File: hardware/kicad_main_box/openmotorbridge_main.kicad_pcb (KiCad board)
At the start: 4 copper layers, 85 x 55 mm, 40 parts, among them J1 DEUTSCH_DTM12_HEADER_SMD, J2 MicroSD_Card, J3 USB2_IDC_HEADER_9PIN, J4 RGB_LED_3PIN, J5 PWR_BAT_NTC_4PIN, SW1 SW_PAIR_RESET, U1 LM5164-Q1, U2 ESP32-S3-WROOM-1U-N16R8, U3 ES8388_Codec, U5 BMI270_IMU, U6 TCAN334G, U7 SX1262IMLTRT, U8 DW3110, U9 TPS7A0533_LDO, Y1_UWB 38.4MHz

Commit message: hardware(main-box): replace J1 open pinheader with official shrouded IDC box header (Wannenstecker)
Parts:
- J1: value DEUTSCH_DTM12_HEADER_SMD -> DEUTSCH_DTM12_IDC_HEADER; footprint Connector_PinHeader_2.54mm:PinHeader_2x06_P2.54mm_Vertical_SMD -> Connector_IDC:IDC-Header_2x06_P2.54mm_Vertical

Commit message: feat(audio): genuinely integrate Qualcomm QCC3084 BT 5.4 Audio SoC for dual-helmet aptX HD link
- Hardware (PCBA 01): Placed U9 (Qualcomm QCC3084 module with onboard ceramic antenna) at (175, 106) on F.Cu; wired I2S bus, UART, and reset/enable controls in mcu_codec_can.kicad_sch.
- Firmware: Upgraded bluetooth_audio_manager to full QCC3084 driver supporting Dual-A2DP aptX HD/Adaptive, LE Audio Auracast, independent AVRCP volume, and modal HFP 1.8 telephony interceptor.
- Docs: Updated 02_intercom_matrix_profiles, 07_pcba_hardware_pinouts, and 09_firmware_architecture with technical specs and pinout tables for the dedicated Qualcomm audio link.
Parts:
- added U9: QCC3084_BT54_AUDIO, RF_Module:Qualcomm_QCC3084_Module, F.Cu at (175.0, 106.0)
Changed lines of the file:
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@@
+		)
+	)
+	(footprint "RF_Module:Qualcomm_QCC3084_Module"
+		(layer "F.Cu")
+		(at 175 106)
+		(descr "Qualcomm QCC3084 Bluetooth 5.4 Audio SoC Module (Dual-A2DP aptX-HD, LE Audio Auracast, HFP 1.8), 13x18mm with integrated ceramic antenna")
+		(tags "Qualcomm QCC3084 Bluetooth 5.4 aptX HD Audio Module")
+		(property "Reference" "U9"
+			(at 0 -10.2 0)
+			(layer "F.SilkS")
+			(effects
+				(font
+					(size 0.8 0.8)
+					(thickness 0.12)
+				)
+			)
+		)
+		(property "Value" "QCC3084_BT54_AUDIO"
+			(at 0 10.2 0)
+			(layer "F.Fab")
+			(effects
+				(font
+					(size 0.8 0.8)
+					(thickness 0.12)
+				)
+			)
+		)
+		(property "Datasheet" "https://www.qualcomm.com/products/application/audio/qcc3084"
+			(at 0 0 0)
+			(layer "F.Fab")
+			(hide yes)
+			(effects
+				(font
+					(size 1.27 1.27)
+				)
+			)
+		)
+		(property "Description" "Qualcomm QCC3084 Dual-A2DP aptX HD / LE Audio Auracast BT 5.4 Module"
+			(at 0 0 0)
+			(layer "F.Fab")
+			(hide yes)
+			(effects
+				(font
+					(size 1.27 1.27)
+				)
+			)
+		)
+		(property "LCSC" "C983084"
+			(at 0 0 0)
+			(layer "F.SilkS")
+			(effects
+				(font
+					(size 1.27 1.27)
+					(thickness 0.15)
+				)
+			)
+		)
+		(attr smd)
+		(duplicate_pad_numbers_are_jumpers no)
+		(fp_rect
+			(start -6.5 -9)
+			(end 6.5 9)
+			(stroke
+				(width 0.15)
+				(type solid)
+			)
+			(fill no)
+			(layer "F.SilkS")
+		)
+		(fp_rect
+			(start 3.5 -8)
+			(end 6 -4.5)
+			(stroke
+				(width 0.12)
+				(type solid)
+			)
+			(fill yes)
+			(layer "F.SilkS")
+		)
+		(fp_rect
+			(start -6.8 -9.3)
+			(end 6.8 9.3)
+			(stroke
+				(width 0.05)
+				(type solid)
+			)
+			(fill no)
+			(layer "F.CrtYd")
+		)
+		(fp_text user "CERAMIC_ANT"
+			(at 4.75 -2.5 90)
+			(layer "F.SilkS")
+			(effects
+				(font
+					(size 0.6 0.6)
+					(thickness 0.1)
+				)
+			)
+		)
+		(fp_text user "${REFERENCE}"
+			(at 0 0 0)
+			(layer "F.Fab")
+			(effects
+				(font
+					(size 0.8 0.8)
+					(thickness 0.12)
+				)
+			)
+		)
+		(pad "1" smd rect
+			(at -6.2 -6)
+			(size 1.4 0.8)
+			(layers "F.Cu" "F.Mask" "F.Paste")
+			(net "VCC_3V3")
+		)
+		(pad "2" smd rect
+			(at -6.2 -4)
+			(size 1.4 0.8)
+			(layers "F.Cu" "F.Mask" "F.Paste")
+			(net "GND_PWR")
+		)
+		(pad "3" smd rect
+			(at -6.2 -2)
+			(size 1.4 0.8)
+			(layers "F.Cu" "F.Mask" "F.Paste")
+			(net "I2S_MCLK")
+		)
+		(pad "4" smd rect
+			(at -6.2 0)
+			(size 1.4 0.8)
+			(layers "F.Cu" "F.Mask" "F.Paste")
+			(net "I2S_BCLK")
+		)
+		(pad "5" smd rect
+			(at -6.2 2)
+			(size 1.4 0.8)
+			(layers "F.Cu" "F.Mask" "F.Paste")
+			(net "I2S_WS")
+		)
+		(pad "6" smd rect
+			(at -6.2 4)
+			(size 1.4 0.8)
+			(layers "F.Cu" "F.Mask" "F.Paste")
+			(net "I2S_DOUT")
+		)
+		(pad "7" smd rect
+			(at -6.2 6)
+			(size 1.4 0.8)
+			(layers "F.Cu" "F.Mask" "F.Paste")
+			(net "I2S_DIN")
+		)
+		(pad "8" smd rect
+			(at 6.2 6)
+			(size 1.4 0.8)
+			(layers "F.Cu" "F.Mask" "F.Paste")
+			(net "GND_PWR")
+		)
+		(pad "9" smd rect
+			(at 6.2 4)
+			(size 1.4 0.8)
+			(layers "F.Cu" "F.Mask" "F.Paste")
+			(net "BT_UART_TX")
+		)
+		(pad "10" smd rect
+			(at 6.2 2)
+			(size 1.4 0.8)
+			(layers "F.Cu" "F.Mask" "F.Paste")
+			(net "BT_UART_RX")
+		)
+		(pad "11" smd rect
+			(at 6.2 0)
+			(size 1.4 0.8)
+			(layers "F.Cu" "F.Mask" "F.Paste")
+			(net "BT_EN")
+		)
+		(pad "12" smd rect
+			(at 6.2 -2)
+			(size 1.4 0.8)
+			(layers "F.Cu" "F.Mask" "F.Paste")
+			(net "GND_PWR")
+		)
+		(embedded_fonts no)
+		(model "${KICAD10_3DMODEL_DIR}/RF_Module.3dshapes/Raytac_MDBT50Q.step"
+			(offset
+				(xyz 0 0 0)
+			)
+			(scale
+				(xyz 1.25 1 1.2)
+			)
+			(rotate
+				(xyz 0 0 0)
+			)
 		)
 	)

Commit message: hardware(cartridge): move ES8388 audio codec to B.Cu bottom layer to eliminate overlaps and isolate from actuator MOSFETs
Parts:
- moved ANT2 17.6 mm to (169.2, 99.7)
- moved U9 6.75 mm to (181.4, 104.0)
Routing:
- net GND_SHIELD: track 0.00 -> 171.1 mm, vias 0 -> 4
- net I2S_WS: track 0.00 -> 7.18 mm
- net USB_D_N: track 0.00 -> 3.96 mm
- net I2S_BCLK: track 0.00 -> 3.11 mm
- net POD2_VCC: track 0.00 -> 2.60 mm
- net VCC_5V: track 0.00 -> 2.04 mm
- net I2S_DOUT: track 0.00 -> 0.71 mm
- net I2S_DIN: track 0.00 -> 0.71 mm

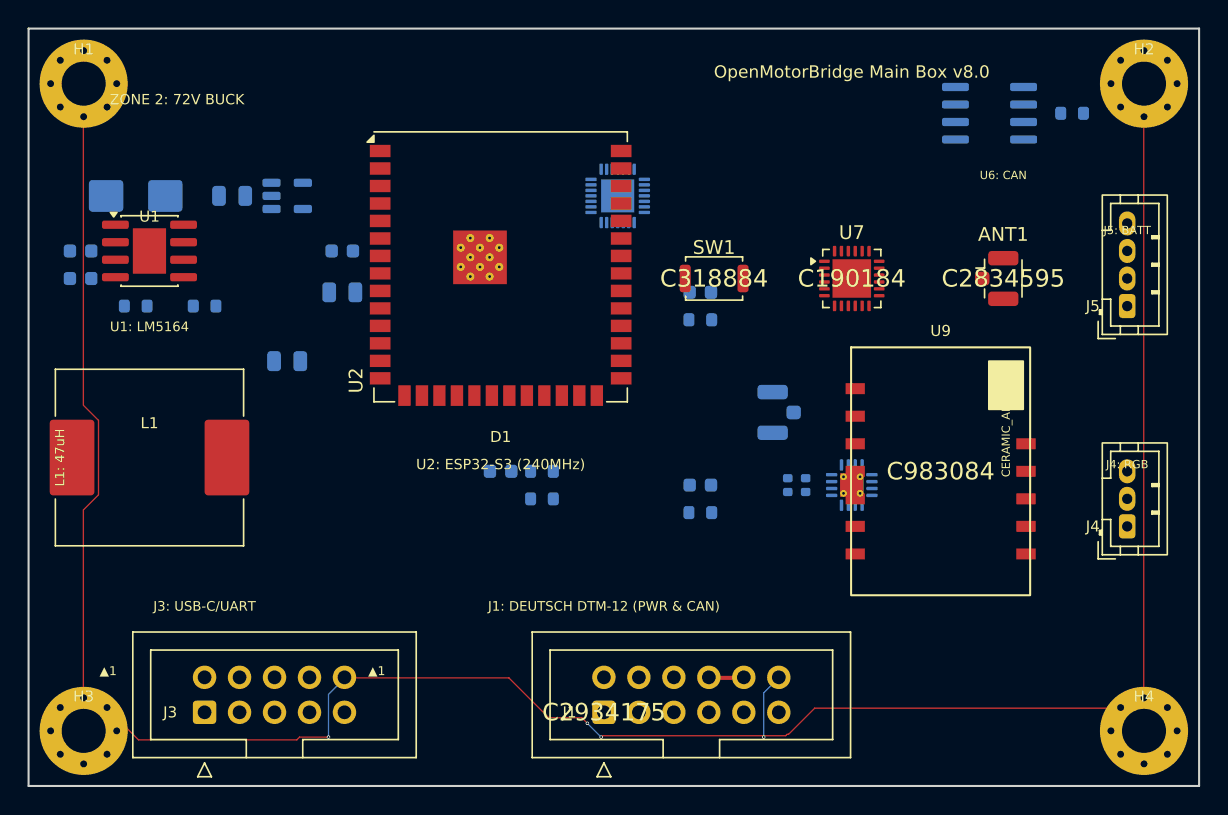
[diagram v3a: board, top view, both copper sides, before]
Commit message: fix(main_box): clean up schematics, connect LoRa/UWB/IMU/SD/LED nets, verify J2 MicroSD placement
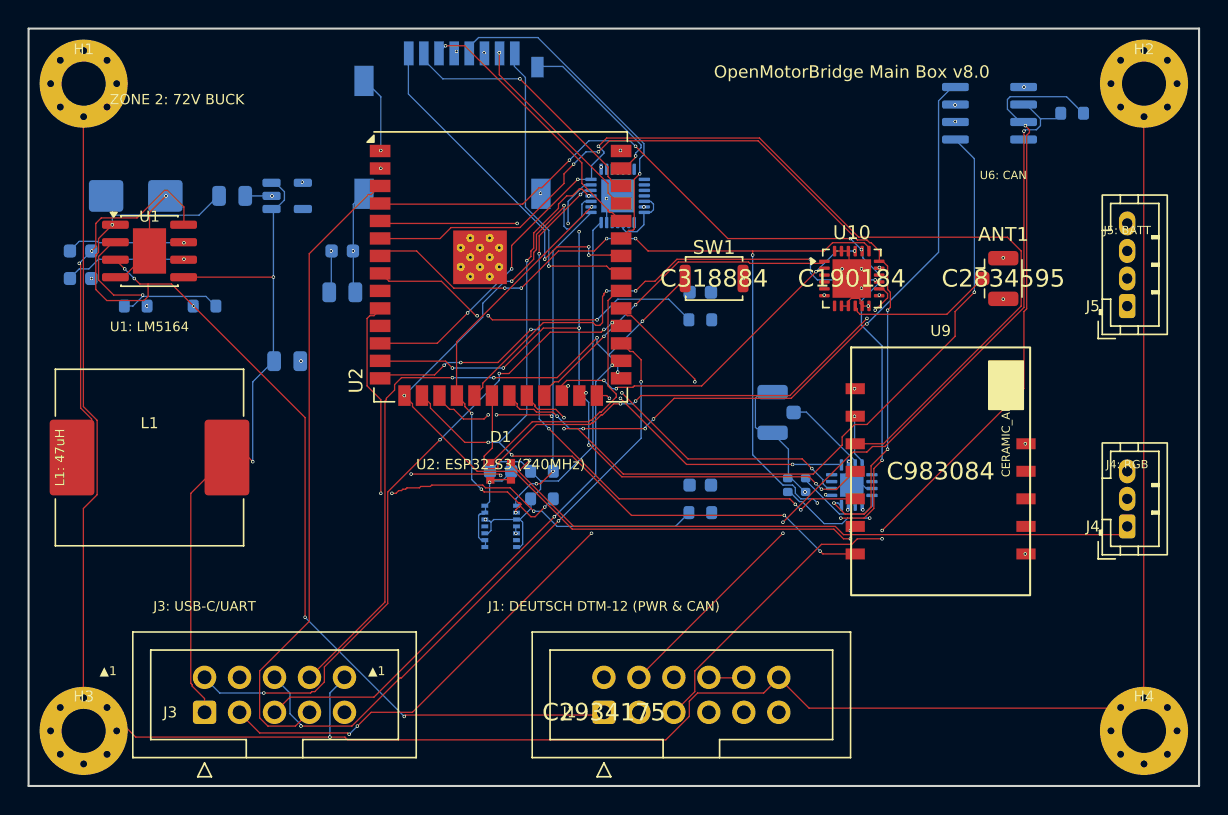
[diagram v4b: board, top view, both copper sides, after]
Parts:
- J2: footprint Connector_Card:microSD_HC_Molex_47571-0001 -> Connector_Card:microSD_HC_Hirose_DM3D-SF
- moved J2 22.5 mm to (146.0, 79.0), turned to 180 degrees
- renumbered U7 to U10, U9 to U11
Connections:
- ANT1 pad 1: (no net) -> LORA_RF_868
- ANT1 pad 2: (no net) -> GND_PWR
- ANT2 pad 1: (no net) -> UWB_RF_CH5
- ANT2 pad 2: (no net) -> GND_PWR
- SW1 pad 1: (no net) -> ESP_BOOT
- SW1 pad 2: (no net) -> GND_PWR
- U10 pad : (no net) -> GND_PWR
- U10 pad 1: (no net) -> LORA_RST
- U10 pad 10: (no net) -> LORA_RF_868
- U10 pad 11: (no net) -> GND_PWR
- U10 pad 12: (no net) -> GND_PWR
- U10 pad 13: (no net) -> VCC_3V3
- U10 pad 14: (no net) -> LORA_BUSY
- U10 pad 15: (no net) -> LORA_DIO1
- U10 pad 16: (no net) -> LORA_DIO2
- U10 pad 17: (no net) -> VCC_3V3
- U10 pad 18: (no net) -> SPI_MISO
- U10 pad 19: (no net) -> SPI_MOSI
- U10 pad 2: (no net) -> LORA_XTA
- U10 pad 20: (no net) -> SPI_SCK
- U10 pad 21: (no net) -> LORA_NSS
- U10 pad 22: (no net) -> GND_PWR
- U10 pad 23: (no net) -> GND_PWR
- U10 pad 24: (no net) -> GND_PWR
- U10 pad 25: (no net) -> GND_PWR
- U10 pad 3: (no net) -> LORA_XTB
- U10 pad 4: (no net) -> LORA_VR_DCDC
- U10 pad 5: (no net) -> LORA_DCC_SW
- U10 pad 6: (no net) -> VCC_3V3
- U10 pad 7: (no net) -> LORA_VR_PA
- U10 pad 8: (no net) -> GND_PWR
- U10 pad 9: (no net) -> GND_PWR
- U2 pad 19: POD3_UART_RX -> LORA_DIO1
- U2 pad 20: POD3_UART_TX -> LORA_BUSY
- U2 pad 23: POD3_GNSS_PPS -> LORA_RST
- U2 pad 24: ONEWIRE_ID -> LORA_NSS
- U2 pad 25: RESERVE_GPIO_A -> UWB_CS
- U2 pad 26: RESERVE_GPIO_B -> UWB_IRQ
- U2 pad 27: STATUS_LED_MCU -> ESP_BOOT
- U2 pad 32: (no net) -> RGB_LED_DATA
- U2 pad 33: (no net) -> SD_DAT1
- U2 pad 34: (no net) -> SD_DAT2
- U2 pad 35: (no net) -> SD_CLK
- U2 pad 36: (no net) -> SD_CMD
- U2 pad 37: (no net) -> SD_DAT0
- U2 pad 38: (no net) -> SD_DAT3
- U2 pad 39: (no net) -> SD_CD
- U2 pad 4: ADC_BAT -> SPI_SCK
- U2 pad 6: ADC_LINE_LVL -> SPI_MISO
- U2 pad 7: ADC_VIGN -> SPI_MOSI
- U8 pad : (no net) -> GND_PWR
- U8 pad 1: (no net) -> VCC_1V8
- U8 pad 10: (no net) -> UWB_CS
- U8 pad 11: (no net) -> UWB_WAKE
- U8 pad 12: (no net) -> UWB_RST
- U8 pad 13: (no net) -> UWB_IRQ
- U8 pad 14: (no net) -> VCC_3V3
- U8 pad 15: (no net) -> UWB_RF_CH5
- U8 pad 16: (no net) -> GND_PWR
- U8 pad 17: (no net) -> GND_PWR
- U8 pad 2: (no net) -> VCC_1V2
- U8 pad 3: (no net) -> GND_PWR
- U8 pad 4: (no net) -> UWB_XTAL1
- U8 pad 5: (no net) -> UWB_XTAL2
- U8 pad 6: (no net) -> GND_PWR
- U8 pad 7: (no net) -> SPI_SCK
- U8 pad 8: (no net) -> SPI_MISO
- U8 pad 9: (no net) -> SPI_MOSI
- Y1_UWB pad 1: (no net) -> UWB_XTAL1
- Y1_UWB pad 3: (no net) -> UWB_XTAL2
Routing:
- net VCC_5V: track 2.04 -> 120.0 mm, vias 0 -> 5
- net GND_PWR: track 0.00 -> 88.8 mm, vias 0 -> 26
- net I2S_MCLK: track 0.00 -> 83.9 mm, vias 0 -> 4
- net KL30_IN: track 0.00 -> 81.5 mm, vias 0 -> 6
- net I2S_DIN: track 0.71 -> 69.2 mm, vias 0 -> 6
- net I2S_DOUT: track 0.71 -> 69.1 mm, vias 0 -> 5
- net SPI_MISO: track 0.00 -> 67.1 mm, vias 0 -> 5
- net SPI_SCK: track 0.00 -> 65.1 mm, vias 0 -> 7
- net CAN_L: track 0.00 -> 64.5 mm, vias 0 -> 3
- net CAN_TX: track 0.00 -> 63.6 mm, vias 0 -> 5
- net SPI_MOSI: track 0.00 -> 61.9 mm, vias 0 -> 7
- net I2S_BCLK: track 3.11 -> 63.3 mm, vias 0 -> 8
- net CAN_H: track 0.00 -> 57.1 mm, vias 0 -> 3
- net USB_D_P: track 0.00 -> 55.0 mm, vias 0 -> 4
- net ESP_BOOT: track 0.00 -> 54.2 mm, vias 0 -> 5
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
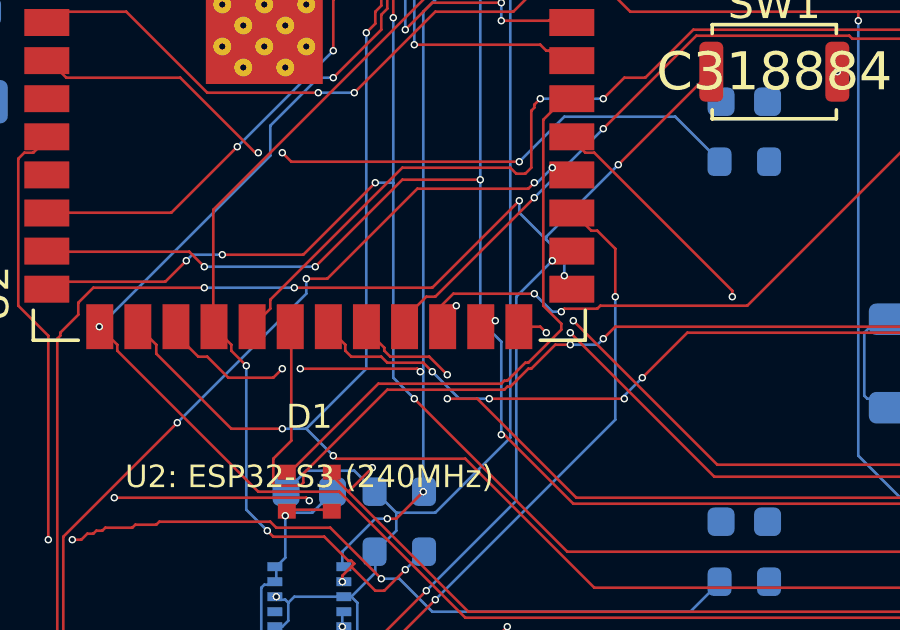
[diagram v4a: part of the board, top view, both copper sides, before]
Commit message: fix(main_box): remove obsolete ONEWIRE_ID stub at Pin 24 to eliminate DRC shorts
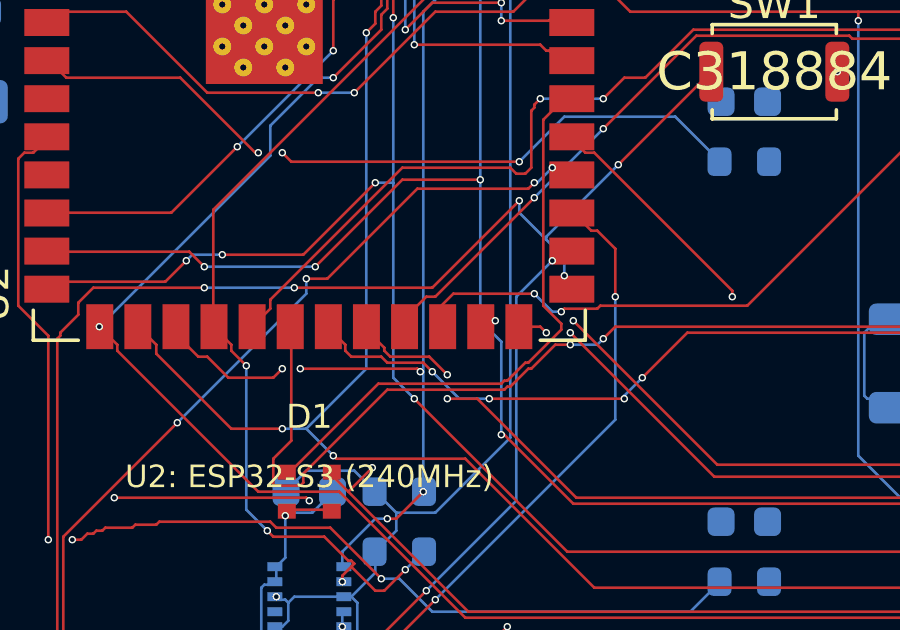
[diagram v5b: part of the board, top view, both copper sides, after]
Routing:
- net ONEWIRE_ID: track 24.4 -> 17.2 mm, vias 2 -> 1
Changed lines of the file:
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@@
-	)
-	(segment
-		(start 153.9 98.3)
-		(end 153.9 98.5)
-		(width 0.0889)
-		(layer "F.Cu")
-		(net "ONEWIRE_ID")
 	)
 	(segment
@@
 	)
 	(segment
-		(start 153.9 98.5)
-		(end 153.945 98.5)
-		(width 0.0889)
-		(layer "F.Cu")
-		(net "ONEWIRE_ID")
-	)
-	(segment
 		(start 141.1 86.1)
 		(end 141.3 86.1)
-		(width 0.0889)
-		(layer "F.Cu")
-		(net "ONEWIRE_ID")
-	)
-	(segment
-		(start 154.4 97.8)
-		(end 153.9 98.3)
 		(width 0.0889)
 		(layer "F.Cu")
@@
 	)
 	(via
-		(at 154.4 97.8)
-		(size 0.25)
-		(drill 0.15)
-		(layers "F.Cu" "B.Cu")
-		(net "ONEWIRE_ID")
-	)
-	(via
 		(at 150.7 86)
 		(size 0.25)
@@
 		(net "ONEWIRE_ID")
 	)
-	(segment
-		(start 154.4 96.8)
-		(end 154.4 97.8)
-		(width 0.0889)
-		(layer "In1.Cu")
-		(net "ONEWIRE_ID")
-	)
-	(segment
-		(start 150.7 93.1)
-		(end 154.4 96.8)
-		(width 0.0889)
-		(layer "In1.Cu")
-		(net "ONEWIRE_ID")
-	)

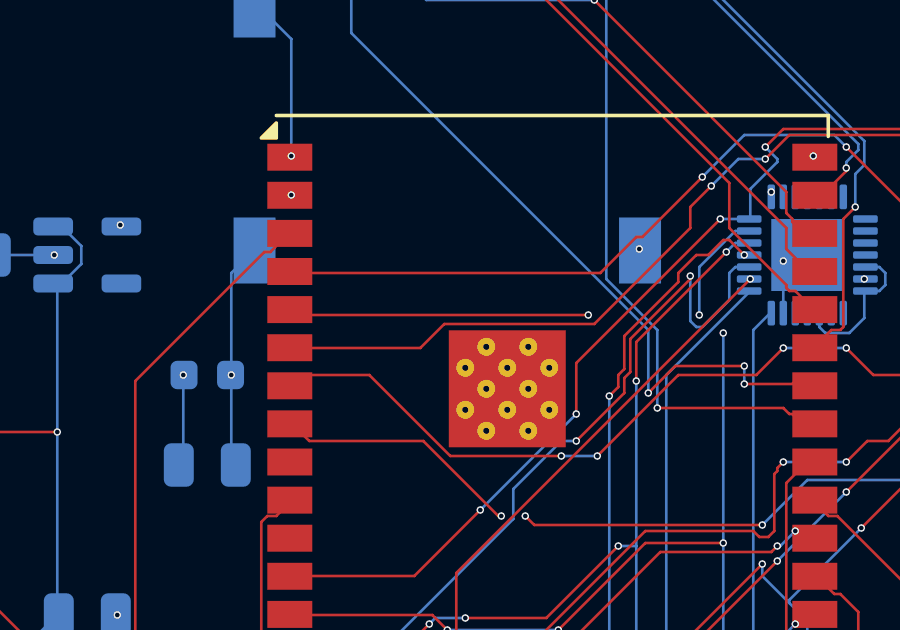
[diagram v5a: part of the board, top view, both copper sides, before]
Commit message: fix(pcb): eliminate all 12 unconnected nets and inner-plane orphan stubs on Central Main Box (PCBA 01)
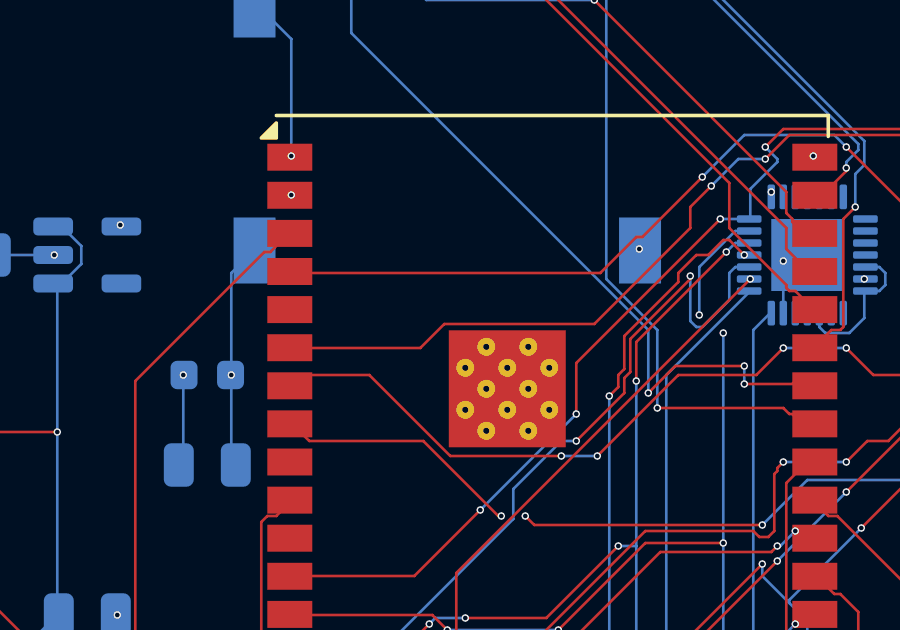
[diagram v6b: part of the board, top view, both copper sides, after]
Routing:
- net ONEWIRE_ID: track 17.2 -> 0.82 mm, vias 1 -> 0
- net CAN_TX: track 63.6 -> 50.3 mm
- net LORA_BUSY: track 52.9 -> 41.3 mm
- net I2S_DIN: track 69.2 -> 58.6 mm
- net I2S_DOUT: track 69.1 -> 61.8 mm
- net I2S_BCLK: track 63.3 -> 57.7 mm
- net I2S_MCLK: track 83.9 -> 78.9 mm
- net UART_RXD0: track 49.5 -> 45.4 mm
- net ESP_BOOT: track 54.2 -> 51.5 mm
- net KL30_IN: track 81.5 -> 78.9 mm
- net USB_D_N: track 48.5 -> 47.6 mm
- net USB_D_P: track 55.0 -> 54.2 mm
- net SPI_MISO: track 67.1 -> 66.5 mm

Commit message: feat: sync re-routed PCBAs (01, 03, 07, 08, 10), manufacturing packages, 3D renders & docs
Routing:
- net I2S_MCLK: track 78.9 -> 50.1 mm, vias 4 -> 6
- net SPI_SCK: track 65.1 -> 79.7 mm, vias 7 -> 6
- net SPI_MISO: track 66.5 -> 78.9 mm, vias 5 -> 6
- net USB_D_P: track 54.2 -> 42.4 mm, vias 4 -> 5
- net GND_PWR: track 88.8 -> 80.3 mm, vias 26 -> 23
- net UART_RXD0: track 45.4 -> 37.3 mm
- net CAN_TX: track 50.3 -> 42.8 mm, vias 5 -> 3
- net ESP_BOOT: track 51.5 -> 44.0 mm, vias 5 -> 4
- net PORT2_KEY_MCU: track 38.8 -> 32.0 mm, vias 3 -> 1
- net USB_D_N: track 47.6 -> 40.9 mm, vias 5 -> 4
- net I2S_DOUT: track 61.8 -> 55.9 mm
- net ESP_EN: track 46.7 -> 40.8 mm
- net LORA_BUSY: track 41.3 -> 36.2 mm, vias 4 -> 2
- net CAN_RX: track 54.0 -> 49.0 mm
- net LORA_NSS: track 25.9 -> 30.4 mm, vias 4 -> 2
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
